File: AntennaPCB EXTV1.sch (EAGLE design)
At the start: 28 parts, among them J1 BM02B-ACHSS-GAN-TF(LF)(SN), Q1 27.12MHz

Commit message: Created the layout for routing the External antenna board
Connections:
- removed net SCK: R4.1, U$1.D5/ADR_1/SCK/DTQR
- removed net SDA: R3.1, U$1.SDA/NSS/RX
- net SCLK: now also R4.1, U$1.D5/ADR_1/SCK/DTQR
- net SS: now also R3.1, U$1.SDA/NSS/RX

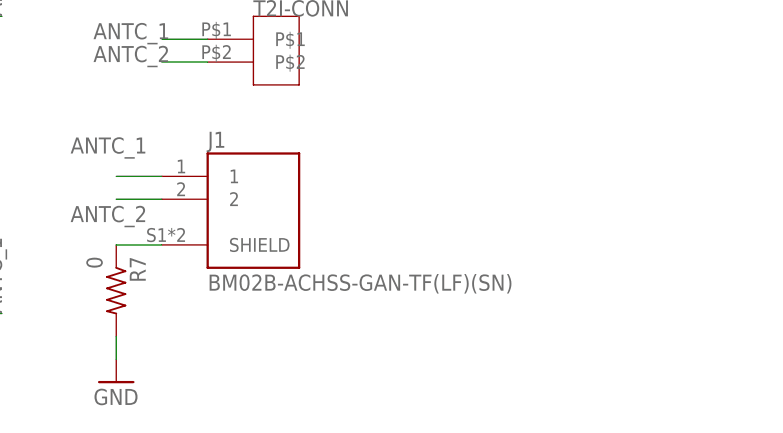
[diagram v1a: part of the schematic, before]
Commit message: Repositioning components on board
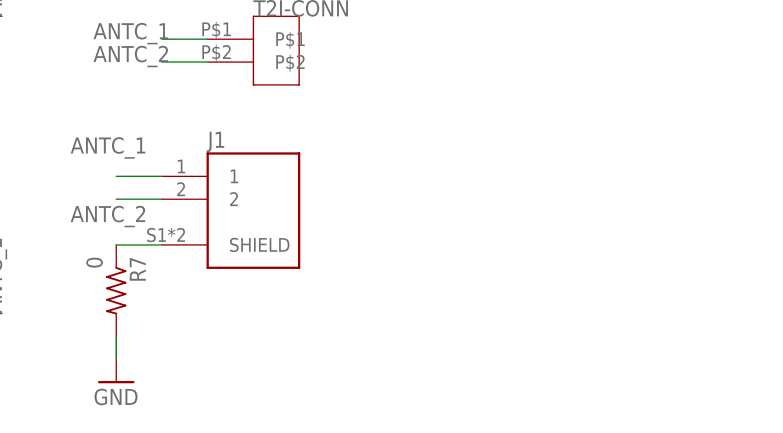
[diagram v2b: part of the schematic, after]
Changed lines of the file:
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@@
 <setting verticaltext="up"/>
 </settings>
-<grid distance="0.1" unitdist="inch" unit="inch" style="lines" multiple="1" display="yes" altdistance="0.01" altunitdist="inch" altunit="inch"/>
+<grid distance="1" unitdist="mm" unit="mm" style="lines" multiple="1" display="no" altdistance="0.01" altunitdist="inch" altunit="inch"/>
 <layers>
-<layer number="1" name="Top" color="4" fill="1" visible="yes" active="no"/>
-<layer number="2" name="Route2" color="16" fill="1" visible="yes" active="no"/>
-<layer number="3" name="Route3" color="17" fill="1" visible="yes" active="no"/>
-<layer number="4" name="Route4" color="18" fill="1" visible="yes" active="no"/>
-<layer number="5" name="Route5" color="19" fill="1" visible="yes" active="no"/>
-<layer number="6" name="Route6" color="25" fill="1" visible="yes" active="no"/>
-<layer number="7" name="Route7" color="26" fill="1" visible="yes" active="no"/>
-<layer number="8" name="Route8" color="27" fill="1" visible="yes" active="no"/>
-<layer number="9" name="Route9" color="28" fill="1" visible="yes" active="no"/>
-<layer number="10" name="Route10" color="29" fill="1" visible="yes" active="no"/>
-<layer number="11" name="Route11" color="30" fill="1" visible="yes" active="no"/>
-<layer number="12" name="Route12" color="20" fill="1" visible="yes" active="no"/>
-<layer number="13" name="Route13" color="21" fill="1" visible="yes" active="no"/>
-<layer number="14" name="Route14" color="22" fill="1" visible="yes" active="no"/>
-<layer number="15" name="Route15" color="23" fill="1" visible="yes" active="no"/>
-<layer number="16" name="Bottom" color="1" fill="1" visible="yes" active="no"/>
-<layer number="17" name="Pads" color="2" fill="1" visible="yes" active="no"/>
-<layer number="18" name="Vias" color="2" fill="1" visible="yes" active="no"/>
-<layer number="19" name="Unrouted" color="6" fill="1" visible="yes" active="no"/>
-<layer number="20" name="Dimension" color="24" fill="1" visible="yes" active="no"/>
-<layer number="21" name="tPlace" color="7" fill="1" visible="yes" active="no"/>
-<layer number="22" name="bPlace" color="7" fill="1" visible="yes" active="no"/>
-<layer number="23" name="tOrigins" color="15" fill="1" visible="yes" active="no"/>
-<layer number="24" name="bOrigins" color="15" fill="1" visible="yes" active="no"/>
-<layer number="25" name="tNames" color="7" fill="1" visible="yes" active="no"/>
-<layer number="26" name="bNames" color="7" fill="1" visible="yes" active="no"/>
-<layer number="27" name="tValues" color="7" fill="1" visible="yes" active="no"/>
-<layer number="28" name="bValues" color="7" fill="1" visible="yes" active="no"/>
+<layer number="1" name="Top" color="4" fill="1" visible="no" active="no"/>
+<layer number="2" name="Route2" color="16" fill="1" visible="no" active="no"/>
+<layer number="3" name="Route3" color="17" fill="1" visible="no" active="no"/>
+<layer number="4" name="Route4" color="18" fill="1" visible="no" active="no"/>
+<layer number="5" name="Route5" color="19" fill="1" visible="no" active="no"/>
+<layer number="6" name="Route6" color="25" fill="1" visible="no" active="no"/>
+<layer number="7" name="Route7" color="26" fill="1" visible="no" active="no"/>
+<layer number="8" name="Route8" color="27" fill="1" visible="no" active="no"/>
+<layer number="9" name="Route9" color="28" fill="1" visible="no" active="no"/>
+<layer number="10" name="Route10" color="29" fill="1" visible="no" active="no"/>
+<layer number="11" name="Route11" color="30" fill="1" visible="no" active="no"/>
+<layer number="12" name="Route12" color="20" fill="1" visible="no" active="no"/>
+<layer number="13" name="Route13" color="21" fill="1" visible="no" active="no"/>
+<layer number="14" name="Route14" color="22" fill="1" visible="no" active="no"/>
+<layer number="15" name="Route15" color="23" fill="1" visible="no" active="no"/>
+<layer number="16" name="Bottom" color="1" fill="1" visible="no" active="no"/>
+<layer number="17" name="Pads" color="2" fill="1" visible="no" active="no"/>
+<layer number="18" name="Vias" color="2" fill="1" visible="no" active="no"/>
+<layer number="19" name="Unrouted" color="6" fill="1" visible="no" active="no"/>
+<layer number="20" name="Dimension" color="24" fill="1" visible="no" active="no"/>
+<layer number="21" name="tPlace" color="7" fill="1" visible="no" active="no"/>
+<layer number="22" name="bPlace" color="7" fill="1" visible="no" active="no"/>
+<layer number="23" name="tOrigins" color="15" fill="1" visible="no" active="no"/>
+<layer number="24" name="bOrigins" color="15" fill="1" visible="no" active="no"/>
+<layer number="25" name="tNames" color="7" fill="1" visible="no" active="no"/>
+<layer number="26" name="bNames" color="7" fill="1" visible="no" active="no"/>
+<layer number="27" name="tValues" color="7" fill="1" visible="no" active="no"/>
+<layer number="28" name="bValues" color="7" fill="1" visible="no" active="no"/>
 <layer number="29" name="tStop" color="7" fill="3" visible="no" active="no"/>
 <layer number="30" name="bStop" color="7" fill="6" visible="no" active="no"/>
@@
 <layer number="35" name="tGlue" color="7" fill="4" visible="no" active="no"/>
 <layer number="36" name="bGlue" color="7" fill="5" visible="no" active="no"/>
-<layer number="37" name="tTest" color="7" fill="1" visible="yes" active="no"/>
-<layer number="38" name="bTest" color="7" fill="1" visible="yes" active="no"/>
+<layer number="37" name="tTest" color="7" fill="1" visible="no" active="no"/>
+<layer number="38" name="bTest" color="7" fill="1" visible="no" active="no"/>
 <layer number="39" name="tKeepout" color="4" fill="11" visible="no" active="no"/>
 <layer number="40" name="bKeepout" color="1" fill="11" visible="no" active="no"/>
@@
 <layer number="44" name="Drills" color="7" fill="1" visible="no" active="no"/>
 <layer number="45" name="Holes" color="7" fill="1" visible="no" active="no"/>
-<layer number="46" name="Milling" color="3" fill="1" visible="yes" active="no"/>
-<layer number="47" name="Measures" color="7" fill="1" visible="yes" active="no"/>
-<layer number="48" name="Document" color="7" fill="1" visible="yes" active="no"/>
-<layer number="49" name="Reference" color="7" fill="1" visible="yes" active="no"/>
-<layer number="50" name="dxf" color="7" fill="1" visible="yes" active="no"/>
-<layer number="51" name="tDocu" color="7" fill="1" visible="yes" active="no"/>
-<layer number="52" name="bDocu" color="7" fill="1" visible="yes" active="no"/>
-<layer number="53" name="tGND_GNDA" color="7" fill="9" visible="yes" active="no"/>
-<layer number="54" name="bGND_GNDA" color="1" fill="9" visible="yes" active="no"/>
-<layer number="56" name="wert" color="7" fill="1" visible="yes" active="no"/>
-<layer number="57" name="tCAD" color="7" fill="1" visible="yes" active="no"/>
-<layer number="59" name="tCarbon" color="7" fill="1" visible="yes" active="no"/>
-<layer number="60" name="bCarbon" color="7" fill="1" visible="yes" active="no"/>
+<layer number="46" name="Milling" color="3" fill="1" visible="no" active="no"/>
+<layer number="47" name="Measures" color="7" fill="1" visible="no" active="no"/>
+<layer number="48" name="Document" color="7" fill="1" visible="no" active="no"/>
+<layer number="49" name="Reference" color="7" fill="1" visible="no" active="no"/>
+<layer number="50" name="dxf" color="7" fill="1" visible="no" active="no"/>
+<layer number="51" name="tDocu" color="7" fill="1" visible="no" active="no"/>
+<layer number="52" name="bDocu" color="7" fill="1" visible="no" active="no"/>
+<layer number="53" name="tGND_GNDA" color="7" fill="9" visible="no" active="no"/>
+<layer number="54" name="bGND_GNDA" color="1" fill="9" visible="no" active="no"/>
+<layer number="56" name="wert" color="7" fill="1" visible="no" active="no"/>
+<layer number="57" name="tCAD" color="7" fill="1" visible="no" active="no"/>
+<layer number="59" name="tCarbon" color="7" fill="1" visible="no" active="no"/>
+<layer number="60" name="bCarbon" color="7" fill="1" visible="no" active="no"/>
 <layer number="88" name="SimResults" color="9" fill="1" visible="yes" active="yes"/>
 <layer number="89" name="SimProbes" color="9" fill="1" visible="yes" active="yes"/>
@@
 <part name="R6" library="Resistor_Capacitor" library_urn="urn:adsk.eagle:library:11396451" deviceset="ERJ-8GEY0R00V" device="" package3d_urn="urn:adsk.eagle:package:10872898/2" value="0"/>
 <part name="U$2" library="SeniorDesignParts" deviceset="T2I-02" device=""/>
-<part name="J1" library="BM02B-ACHSS-GAN-TF_LF__SN_" deviceset="BM02B-ACHSS-GAN-TF(LF)(SN)" device=""/>
+<part name="J1" library="BM02B-ACHSS-GAN-TF_LF__SN_" deviceset="BM02B-ACHSS-GAN-TF(LF)(SN)" device="" value=""/>
 <part name="GND13" library="supply1" library_urn="urn:adsk.eagle:library:371" deviceset="GND" device=""/>
 <part name="R7" library="Resistor_Capacitor" library_urn="urn:adsk.eagle:library:11396451" deviceset="ERJ-8GEY0R00V" device="" package3d_urn="urn:adsk.eagle:package:10872898/2" value="0"/>

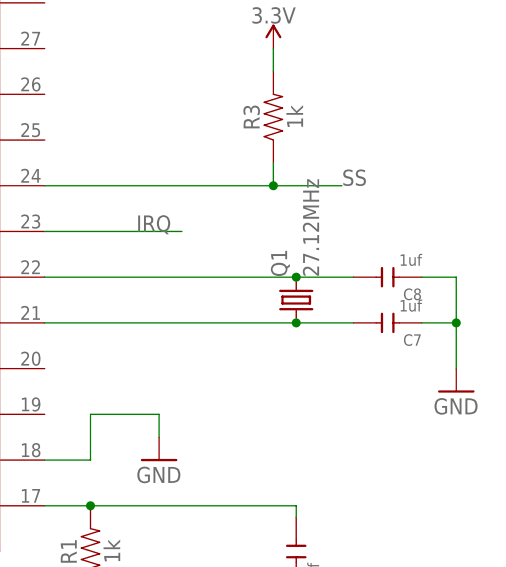
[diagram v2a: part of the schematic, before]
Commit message: Re-created some parts on a schematic and did some more positioning adjustments as well as DRC
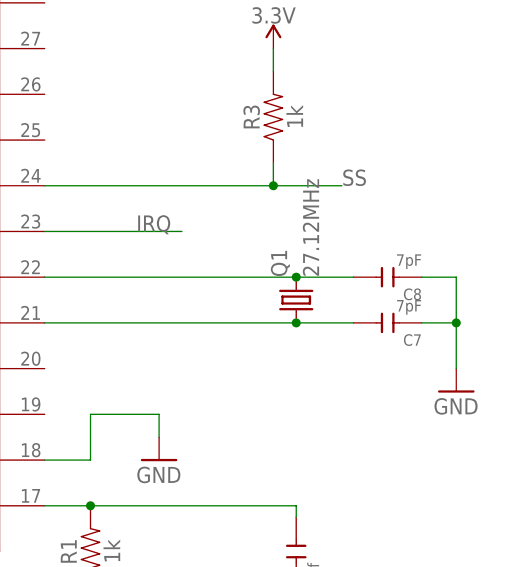
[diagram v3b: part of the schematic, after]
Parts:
- C7, C8: value 1uf -> 7pF
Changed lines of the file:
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@@
 <part name="GND8" library="supply1" library_urn="urn:adsk.eagle:library:371" deviceset="GND" device=""/>
 <part name="Q1" library="crystal" library_urn="urn:adsk.eagle:library:204" deviceset="CRYSTAL" device="HC49S" package3d_urn="urn:adsk.eagle:package:12071/1" value="27.12MHz"/>
-<part name="C7" library="Seeed-Capacitor" library_urn="urn:adsk.eagle:library:464" deviceset="CERAMIC-1UF-25V-10%-X7R(0603)" device="" package3d_urn="urn:adsk.eagle:package:32378/1" value="1uf"/>
-<part name="C8" library="Seeed-Capacitor" library_urn="urn:adsk.eagle:library:464" deviceset="CERAMIC-1UF-25V-10%-X7R(0603)" device="" package3d_urn="urn:adsk.eagle:package:32378/1" value="1uf"/>
+<part name="C7" library="Seeed-Capacitor" library_urn="urn:adsk.eagle:library:464" deviceset="CERAMIC-1UF-25V-10%-X7R(0603)" device="" package3d_urn="urn:adsk.eagle:package:32378/1" value="7pF"/>
+<part name="C8" library="Seeed-Capacitor" library_urn="urn:adsk.eagle:library:464" deviceset="CERAMIC-1UF-25V-10%-X7R(0603)" device="" package3d_urn="urn:adsk.eagle:package:32378/1" value="7pF"/>
 <part name="GND9" library="supply1" library_urn="urn:adsk.eagle:library:371" deviceset="GND" device=""/>
 <part name="L1" library="BeagleBone_Blue_R3" library_urn="urn:adsk.eagle:library:5828899" deviceset="INDUCTOR" device="" package3d_urn="urn:adsk.eagle:package:5829817/3" value="560nH"/>

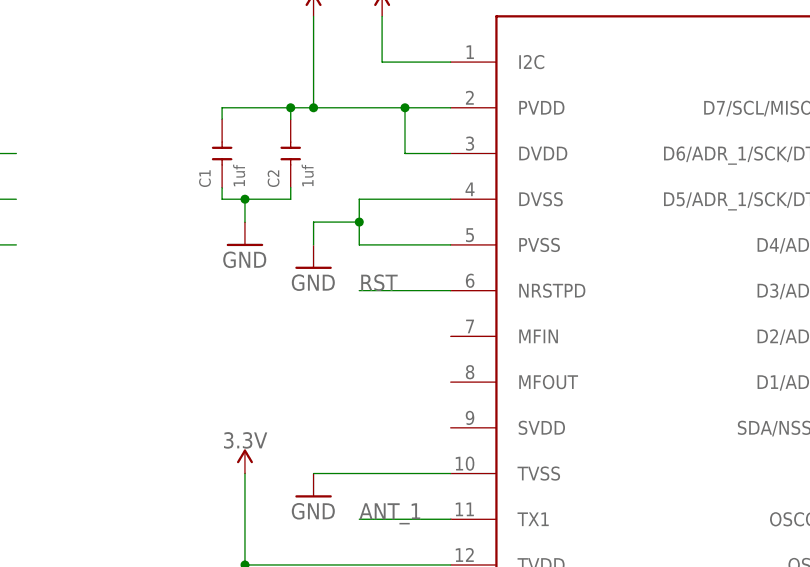
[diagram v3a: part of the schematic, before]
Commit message: Created the antenna board and adjusted sizing of the board
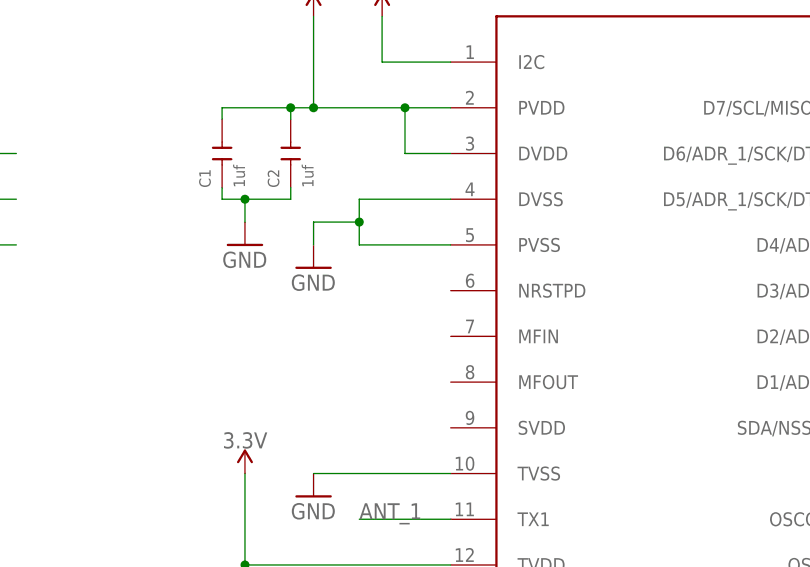
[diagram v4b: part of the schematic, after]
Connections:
- removed net RST: U$1.NRSTPD
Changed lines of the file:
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@@
-</segment>
-</net>
-<net name="RST" class="0">
-<segment>
-<pinref part="U$1" gate="G$1" pin="NRSTPD"/>
-<wire x1="99.06" y1="139.7" x2="88.9" y2="139.7" width="0.1524" layer="91"/>
-<label x="88.9" y="139.7" size="1.778" layer="95"/>
 </segment>
 </net>

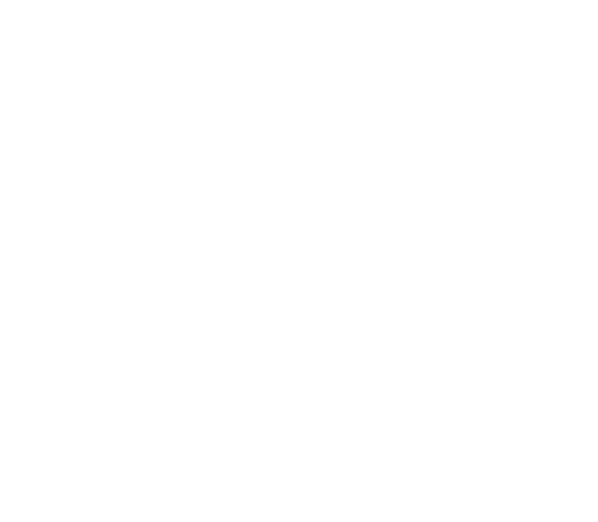
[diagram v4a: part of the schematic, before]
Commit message: Put stand-offs on the board
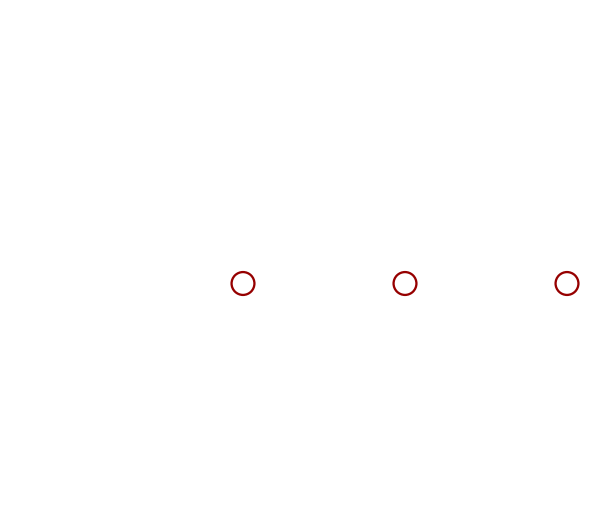
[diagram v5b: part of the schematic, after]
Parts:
- added H1, H2, H3: STAND-OFF, SparkFun-Hardware:STAND-OFF
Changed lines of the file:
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@@
 <part name="GND10" library="supply1" library_urn="urn:adsk.eagle:library:371" deviceset="GND" device=""/>
 <part name="GND11" library="supply1" library_urn="urn:adsk.eagle:library:371" deviceset="GND" device=""/>
+<part name="H1" library="SparkFun-Hardware" library_urn="urn:adsk.eagle:library:519" deviceset="STAND-OFF" device="" package3d_urn="urn:adsk.eagle:package:38630/1"/>
+<part name="H2" library="SparkFun-Hardware" library_urn="urn:adsk.eagle:library:519" deviceset="STAND-OFF" device="" package3d_urn="urn:adsk.eagle:package:38630/1"/>
+<part name="H3" library="SparkFun-Hardware" library_urn="urn:adsk.eagle:library:519" deviceset="STAND-OFF" device="" package3d_urn="urn:adsk.eagle:package:38630/1"/>
 </parts>
 <sheets>
@@
 <attribute name="VALUE" x="93.98" y="22.86" size="1.778" layer="96"/>
 </instance>
+<instance part="H1" gate="G$1" x="184" y="26"/>
+<instance part="H2" gate="G$1" x="202" y="26"/>
+<instance part="H3" gate="G$1" x="220" y="26"/>
 </instances>
 <busses>
